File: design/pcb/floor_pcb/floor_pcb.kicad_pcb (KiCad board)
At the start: 2 copper layers, 75 x 222 mm, 11 parts, among them J1 Conn_01x10_Male, J10 shock_grid, J11 shock_grid, J2 Conn_01x10_Male, J3 DB25_Male, J4 shock_grid, J5 shock_grid, J6 shock_grid, J7 shock_grid, J8 shock_grid, J9 shock_grid

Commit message: Just before adding (this) commit hash to floor and regenerating for manufacture.
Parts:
- added R1.7145mm_NPTH: , R1.7145mm_NPTH, F.Cu at (94.4, 114.5)
- added R1.7145mm_NPTH: , R1.7145mm_NPTH, F.Cu at (94.4, 70.0)
- added R1.7145mm_NPTH: , R1.7145mm_NPTH, F.Cu at (94.4, 160.0)
- added R1.7145mm_NPTH: , R1.7145mm_NPTH, F.Cu at (94.4, 204.5)
- added R1.7145mm_NPTH: , R1.7145mm_NPTH, F.Cu at (155.6, 47.8)
- added R1.7145mm_NPTH: , R1.7145mm_NPTH, F.Cu at (155.6, 92.3)
- added R1.7145mm_NPTH: , R1.7145mm_NPTH, F.Cu at (155.6, 137.8)
- added R1.7145mm_NPTH: , R1.7145mm_NPTH, F.Cu at (155.6, 182.3)
- added R1.7145mm_NPTH: , R1.7145mm_NPTH, F.Cu at (155.6, 204.5)
- added R1.7145mm_NPTH: , R1.7145mm_NPTH, F.Cu at (94.4, 25.8)
- added R1.85178mm_NPTH: , R1.85178mm_NPTH, F.Cu at (125.0, 138.3)
- added R1.85178mm_NPTH: , R1.85178mm_NPTH, F.Cu at (125.0, 93.3)
- added R1.85178mm_NPTH: , R1.85178mm_NPTH, F.Cu at (125.0, 115.8)
- added R1.85178mm_NPTH: , R1.85178mm_NPTH, F.Cu at (125.1, 160.8)
- added R1.85178mm_NPTH: , R1.85178mm_NPTH, F.Cu at (125.0, 48.3)
- added R1.85178mm_NPTH: , R1.85178mm_NPTH, F.Cu at (125.0, 70.8)
- added R1.85178mm_NPTH: , R1.85178mm_NPTH, F.Cu at (125.0, 183.3)
- added R1.85178mm_NPTH: , R1.85178mm_NPTH, F.Cu at (124.9, 25.8)
- added R2.0mm_NPTH: , R2.0mm_NPTH, F.Cu at (105.0, 208.5)
- added R2.0mm_NPTH: , R2.0mm_NPTH, F.Cu at (145.0, 208.5)
- added R2.0mm_NPTH: , R2.0mm_NPTH, F.Cu at (105.0, 15.0)
- added R2.0mm_NPTH: , R2.0mm_NPTH, F.Cu at (145.0, 15.0)
- added R4.2mm_NPTH: , R4.2mm_NPTH, F.Cu at (115.7, 138.3)
- added R4.2mm_NPTH: , R4.2mm_NPTH, F.Cu at (115.6, 93.3)
- added R4.2mm_NPTH: , R4.2mm_NPTH, F.Cu at (134.5, 160.8)
- added R4.2mm_NPTH: , R4.2mm_NPTH, F.Cu at (115.6, 48.3)
- added R4.2mm_NPTH: , R4.2mm_NPTH, F.Cu at (134.3, 70.8)
- added R4.2mm_NPTH: , R4.2mm_NPTH, F.Cu at (134.4, 115.8)
- added R4.2mm_NPTH: , R4.2mm_NPTH, F.Cu at (115.7, 183.3)
- added R4.2mm_NPTH: , R4.2mm_NPTH, F.Cu at (134.3, 25.8)
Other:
- outline, holes or cut-outs redrawn

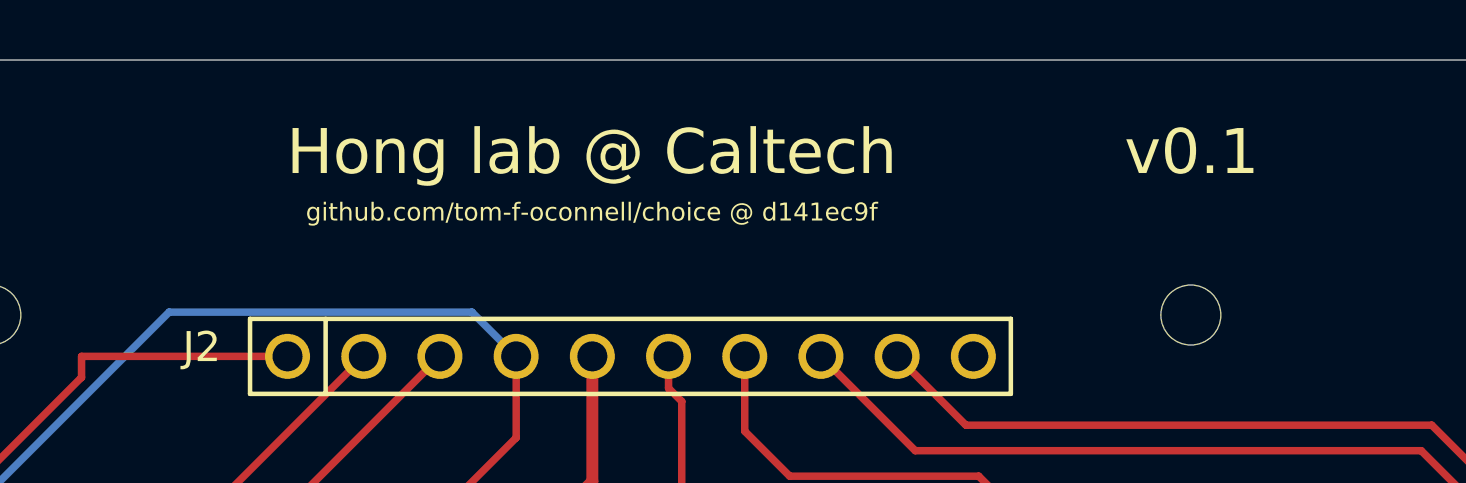
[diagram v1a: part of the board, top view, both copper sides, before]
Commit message: To be submitted for manufacture w/ Advanced Circuits BareBones
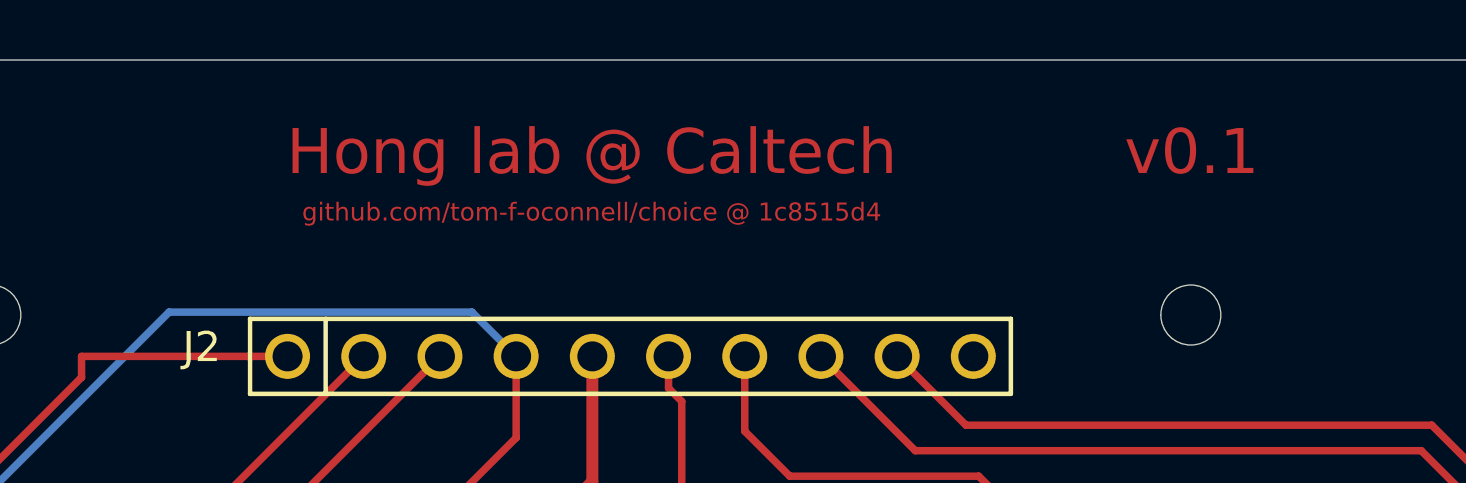
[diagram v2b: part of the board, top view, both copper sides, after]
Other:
- board text added: "github.com/tom-f-oconnell/choice @ 1c8515d4"
- board text removed: "github.com/tom-f-oconnell/choice @ d141ec9f"
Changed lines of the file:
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@@
     (effects (font (size 1.5 1.5) (thickness 0.3)))
   )
-  (gr_text "github.com/tom-f-oconnell/choice @ d141ec9f" (at 125.03 11.58) (layer F.SilkS)
+  (gr_text "github.com/tom-f-oconnell/choice @ 1c8515d4" (at 125.03 11.58) (layer F.Cu)
     (effects (font (size 0.6 0.6) (thickness 0.1)))
   )
-  (gr_text v0.1 (at 145.03 9.58) (layer F.SilkS)
+  (gr_text v0.1 (at 145.03 9.58) (layer F.Cu)
     (effects (font (size 1.5 1.5) (thickness 0.3)))
   )
-  (gr_text "Hong lab @ Caltech" (at 125.03 9.58) (layer F.SilkS)
+  (gr_text "Hong lab @ Caltech" (at 125.03 9.58) (layer F.Cu)
     (effects (font (size 1.5 1.5) (thickness 0.3)))
   )

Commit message: Minor changes to multishock and added notes to board files
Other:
- board text added: "TODO match f_ labels to those in shield (as is w/ v0.1, shield F1 is actually bottom right, F2 is left, ...) maybe change in field to match this?"
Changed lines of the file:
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@@
   (general
     (thickness 1.6)
-    (drawings 42)
+    (drawings 43)
     (tracks 592)
     (zones 0)
@@
       ))
   )
+  (gr_text "TODO match f_ labels to those in shield\n(as is w/ v0.1, shield F1 is actually bottom right, F2 is left, ...)\n\nmaybe change in field to match this?" (at 44.78 41.83) (layer Cmts.User)
+    (effects (font (size 1.5 1.5) (thickness 0.3)))
+  )
   (gr_text "Board should be 1/16\" thick (1.5875 mm)\n\nMight benefit from some kind of gold finish, to lower\ncontact resistance and prevent changes in resistance \ndue to oxidation.\n\nHard gold seems more well suited. Could probably\nwithstand more cleaning cycles. ENIG may be fine." (at 49.53 97.08) (layer Cmts.User)
